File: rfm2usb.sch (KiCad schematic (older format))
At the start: 23 parts, among them J1 USB_B_Micro, J2 DBG, J4 SMA, J5 UART, U1 AP2210N-3.3TRG1, U2 STM32F042K6Tx, U3 RFM69HCW, Y1 8MHz

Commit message: cleanup
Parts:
- removed N1: Housing, Symbol:KiCad-Logo2_5mm_Copper, symbol Mechanical:Housing
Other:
- note added: "3.3V LDO"
- note added: "RF Module"
- note added: "STM32 Micro"
- note added: "SWD Header"
- note added: "UART"
- note added: "USB"
- moved on the sheet: C1, C10, C2, C3, C4, C5, C6, C7, C8, C9, J1, J2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

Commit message: change stm32 footprint
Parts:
- added JP1: SolderJumper_3_Open, Jumper:SolderJumper-3_P1.3mm_Open_RoundedPad1.0x1.5mm_NumberLabels, symbol Jumper:SolderJumper_3_Open
- added N1: Housing, Symbol:KiCad-Logo2_5mm_Copper, symbol Mechanical:Housing
- added R4: 10k, Resistor_SMD:R_0603_1608Metric, symbol Device:R_Small
- U2: value STM32F042K6Tx -> STM32L151CBT; footprint Package_QFP:LQFP-32_7x7mm_P0.8mm -> Package_QFP:LQFP-48_7x7mm_P0.5mm; symbol MCU_ST_STM32F0:STM32F042K6Tx -> MCU_ST_STM32L1:STM32L151CBTxA; Alternative 1 STM32L151CBT -> (none)
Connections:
- net +3V3: now also U2.24 (VDD), U2.36 (VDD), U2.48 (VDD), U2.9 (VDDA), JP1.1 (A); no longer U2.1 (VDD), U2.17 (VDDIO2), U2.5 (VDDA)
- net GND: now also U2.23 (VSS), U2.35 (VSS), U2.47 (VSS), U2.8 (VSSA), JP1.3 (B); no longer C8.2, U2.16 (VSS), U2.32 (VSSA)
- net SPI_CLK: now also U2.15 (PA5); no longer U2.11 (PA5)
- net SPI_MISO: now also U2.16 (PA6); no longer U2.12 (PA6)
- net SPI_MOSI: now also U2.17 (PA7); no longer U2.13 (PA7)
- net SWCLK: now also U2.37 (PA14); no longer U2.24 (PA14)
- net SWDIO: now also U2.34 (PA13); no longer U2.23 (PA13)
- net USART1_RX: now also U2.31 (PA10); no longer U2.20 (PA10)
- net USART1_TX: now also U2.30 (PA9); no longer U2.19 (PA9)
- net USB_D+: now also U2.33 (PA12); no longer U2.22 (PA12)
- net USB_D-: now also U2.32 (PA11); no longer U2.21 (PA11)
- net ~RESET: now also U2.7 (NRST); no longer U2.4 (NRST)
- net ~RFM_IRQ: now also U2.18 (PB0); no longer U2.14 (PB0)
- net ~SPI_SS: now also U2.14 (PA4); no longer U2.10 (PA4)
- net at C9.1, Y1.2: now also U2.5 (PH0); no longer U2.2 (PF0)
- net at C10.1, Y1.1: now also U2.6 (PH1); no longer U2.3 (PF1)
- new net: JP1.2 (C), R4.1
- new net BOOT0: R4.2, U2.44 (BOOT0)
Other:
- note removed: "3.3V LDO"
- note removed: "RF Module"
- note removed: "STM32 Micro"
- note removed: "SWD Header"
- note removed: "UART"
- note removed: "USB"
- moved on the sheet: C1, C10, C2, C5, C9, J1, J2, J4, J5, R1, R2, R3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

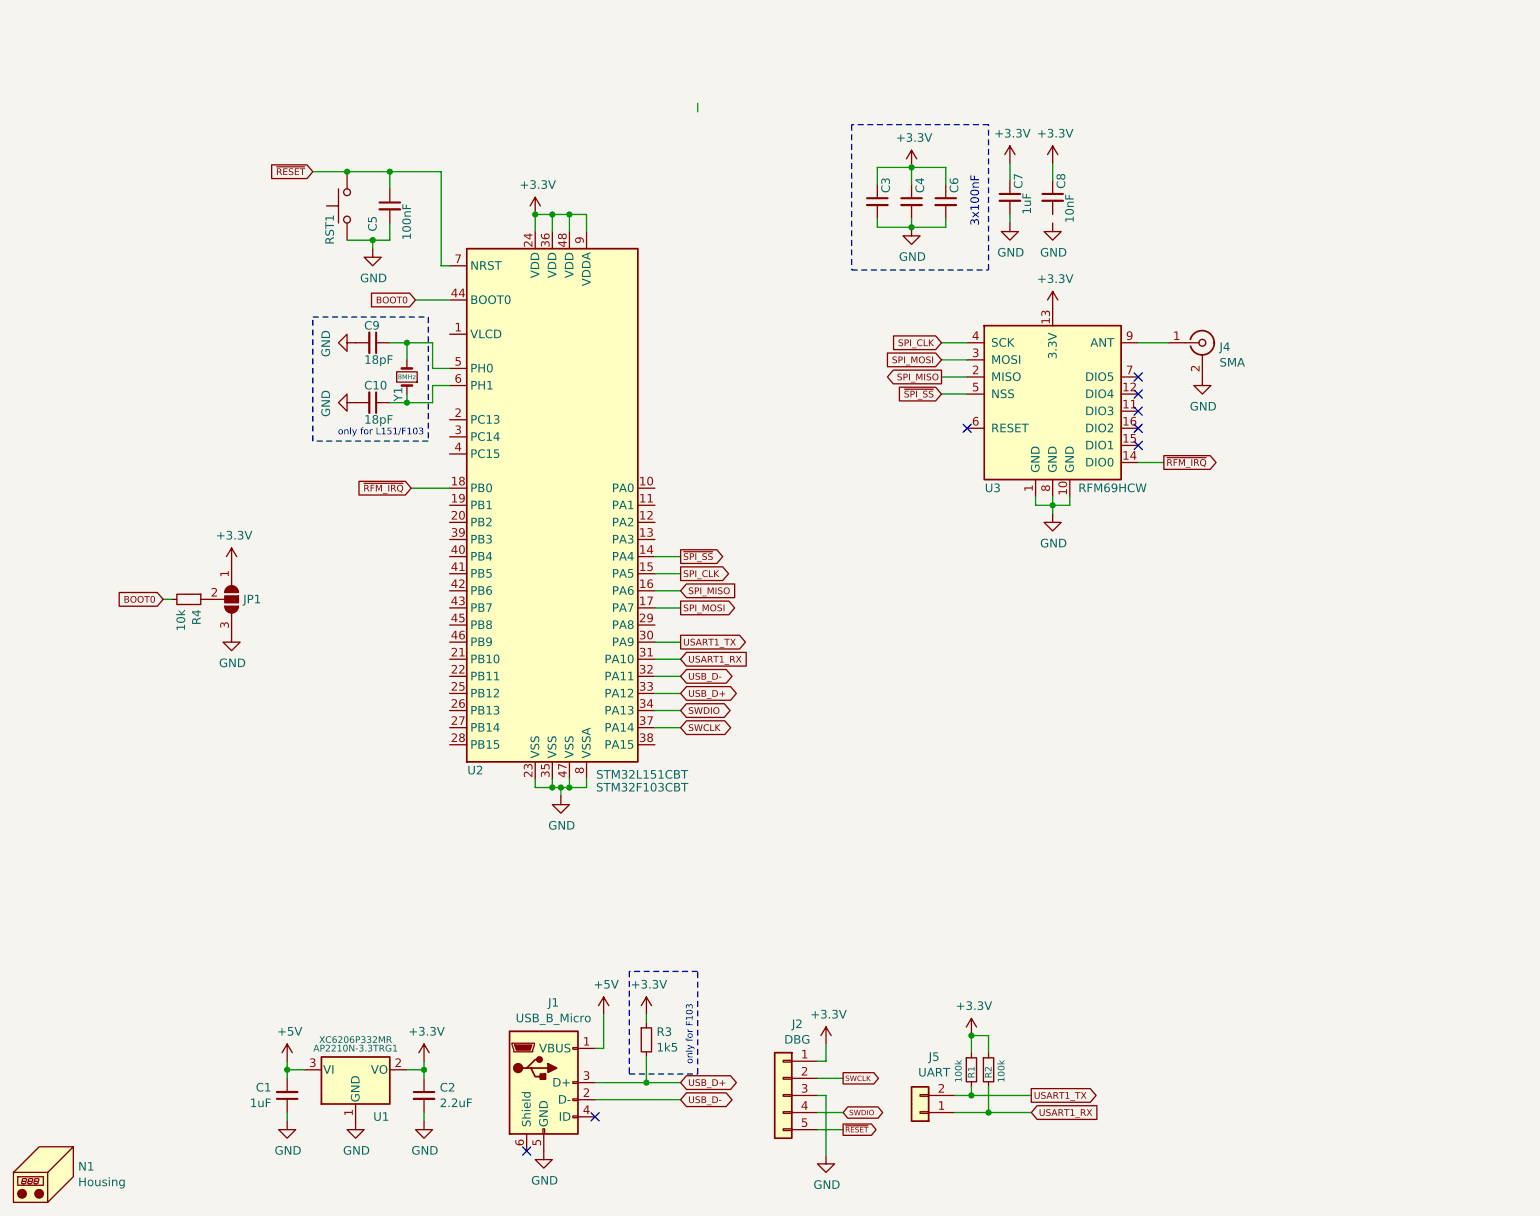
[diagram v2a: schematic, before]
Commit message: replace reset button with boot button this is more useful
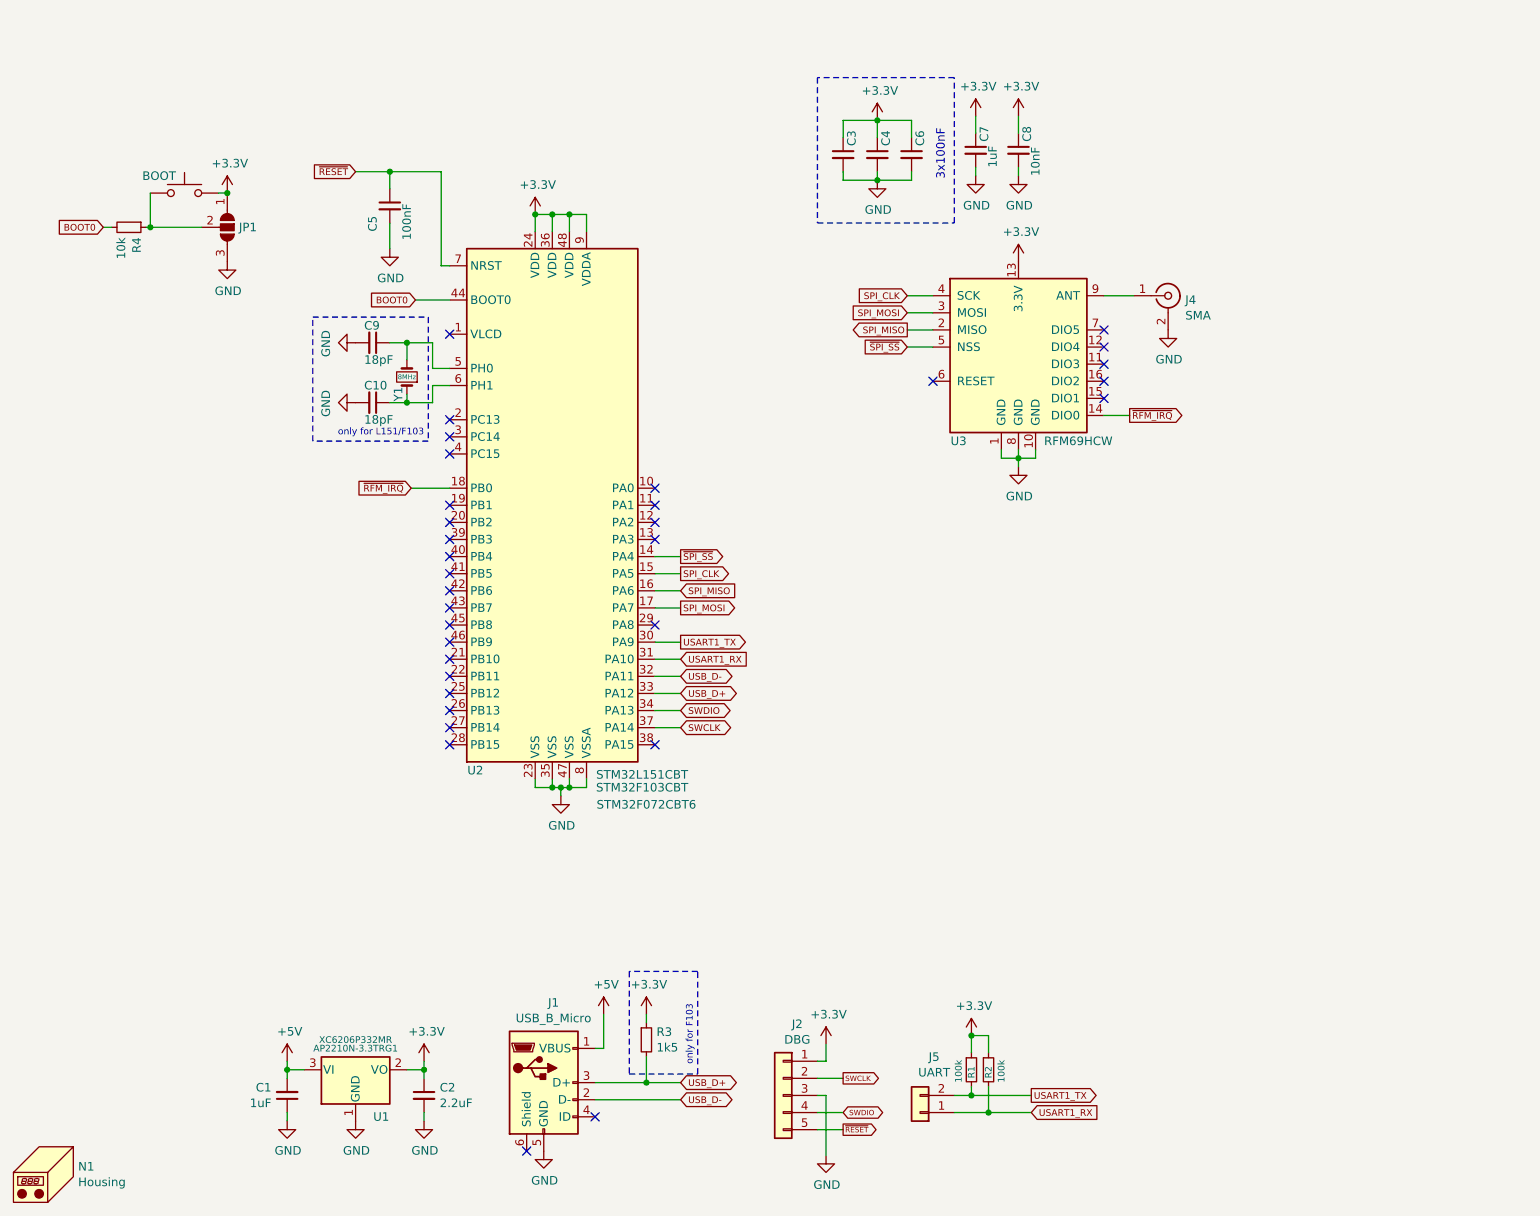
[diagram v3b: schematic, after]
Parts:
- BOOT1: renamed from RST1; value RST -> BOOT
- U2: Alternative (none) -> STM32F072CBT6
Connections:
- net +3V3: now also BOOT1.2
- net GND: now also C8.2; no longer BOOT1.1
- net ~RESET: no longer BOOT1.2
- net at JP1.2 (C), R4.1: now also BOOT1.1
- no-connect marks 8 -> 33
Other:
- moved on the sheet: C3, C4, C6, C7, C8, J4, JP1, R4, U3
